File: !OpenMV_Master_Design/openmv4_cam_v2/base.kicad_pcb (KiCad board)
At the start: 4 copper layers, 35.8 x 44.4 mm, 58 parts, among them J5 XF2M-1015-1A, Q1 BSS138, Q2 Si2301BDS, U1 STM32H743VIT6, U2 OV7725, U5 TPS731XX, U8 PAM2305AABADJ, X2 USD-1040310811, Y1 7S-12.000MAHE-T

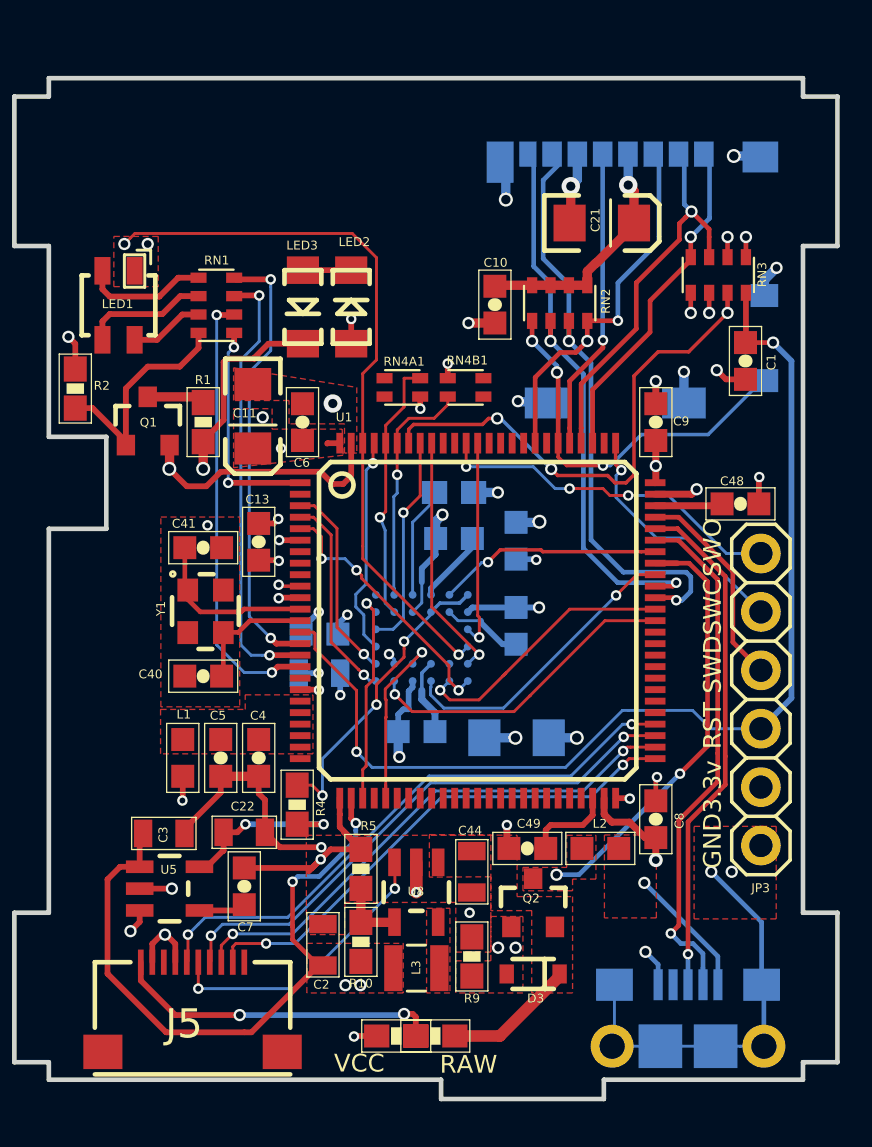
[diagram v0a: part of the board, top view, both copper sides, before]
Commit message: Moved the flat flex connector to suit main board design
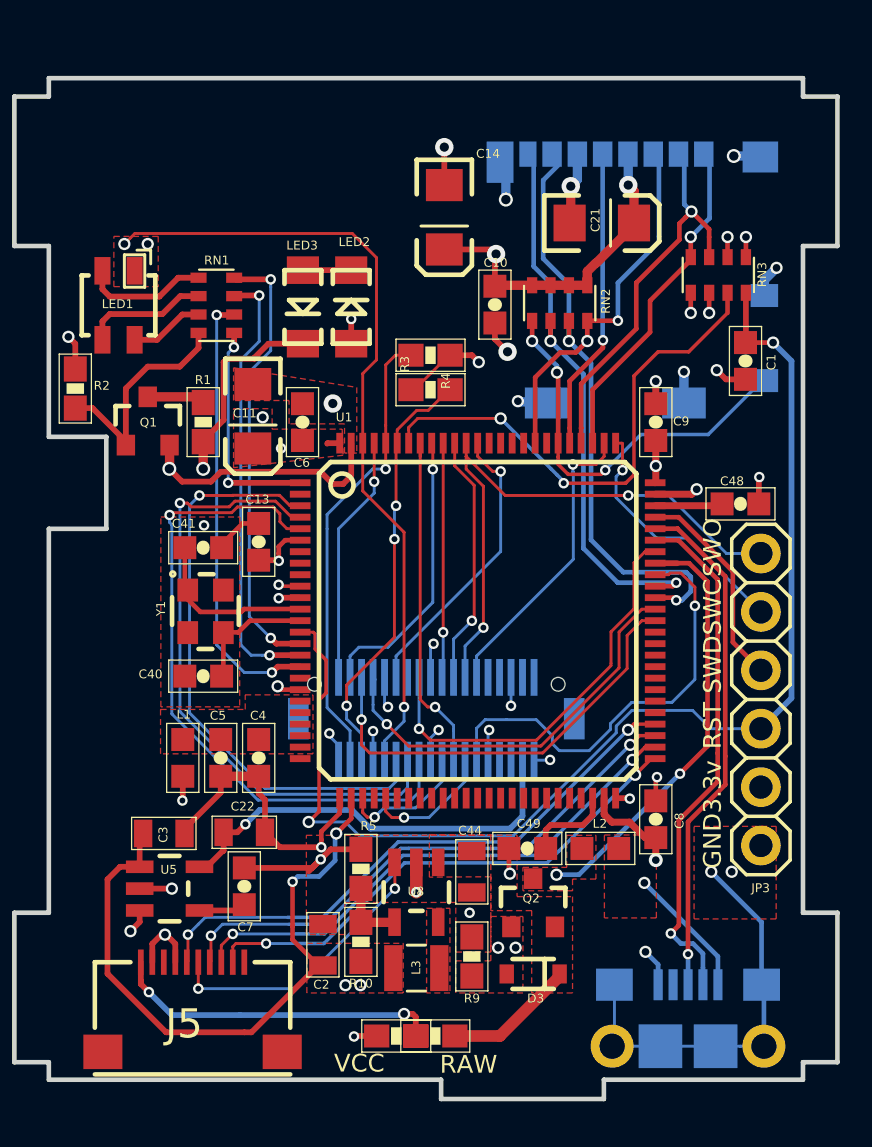
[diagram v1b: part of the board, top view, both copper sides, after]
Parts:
- removed C12: 47uF, openmv3:EIA3216
- removed C15, C16, C17, C19: 0.1uF, openmv3:0603-CAP
- removed C18: 4.7uF, base:0603-CAP
- removed C20: 22uF, openmv3:0805
- removed the R3 at (147.5, 105.3)
- removed the R4 at (140.7, 118.8)
- removed U2: OV7725, openmv3:CSP2-28
- added C14: 47uF, base:EIA3216, F.Cu at (147.1, 93.3)
- added X3: DF12-36-DS, base:DF12-36-DS, B.Cu at (146.7, 115.1)
- R3: renamed from RN4B1; footprint openmv3:EXBV4V -> base:0603-RES
- R4: renamed from RN4A1; footprint openmv3:EXBV4V -> base:0603-RES
- moved R4 1.86 mm to (146.4, 99.3), turned to 180 degrees
- moved R3 1.53 mm to (146.4, 100.8), turned to 0 degrees
- renumbered USB to X1
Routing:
- net /DCMI_D6: track 8.97 -> 27.5 mm
- net /DCMI_D7: track 11.4 -> 28.9 mm, vias 3 -> 1
- net /DCMI_D4: track 8.66 -> 25.6 mm
- net Net-(R4-Pad2): track 13.1 -> 0.00 mm, vias 3 -> 0
- net /SPI3_SSEL: track 0.00 -> 13.1 mm, vias 0 -> 1
- net /SPI3_MISO: track 0.00 -> 10.9 mm, vias 0 -> 1
- net GND: track 83.4 -> 72.7 mm, vias 37 -> 32
- net VDDA: track 7.99 -> 18.7 mm, vias 2 -> 1
- net /SPI3_MOSI: track 0.00 -> 10.2 mm, vias 0 -> 1
- net /SPI3_SCLK/TRACESWO: track 15.4 -> 25.4 mm, vias 3 -> 2
- net VCC: track 58.9 -> 67.8 mm, vias 28 -> 27
- net /I2C1_SDA: track 11.5 -> 20.3 mm
- net /DCMI_RST: track 9.78 -> 18.1 mm
- net /I2C1_SCL: track 10.2 -> 18.6 mm, vias 1 -> 3
- net /NRST: track 47.0 -> 53.3 mm
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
